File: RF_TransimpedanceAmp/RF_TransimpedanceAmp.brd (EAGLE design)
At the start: 22.9 x 22.9 mm, 11 parts, among them IC1 OPA847, IC3 PMA-5452, X1 UMC

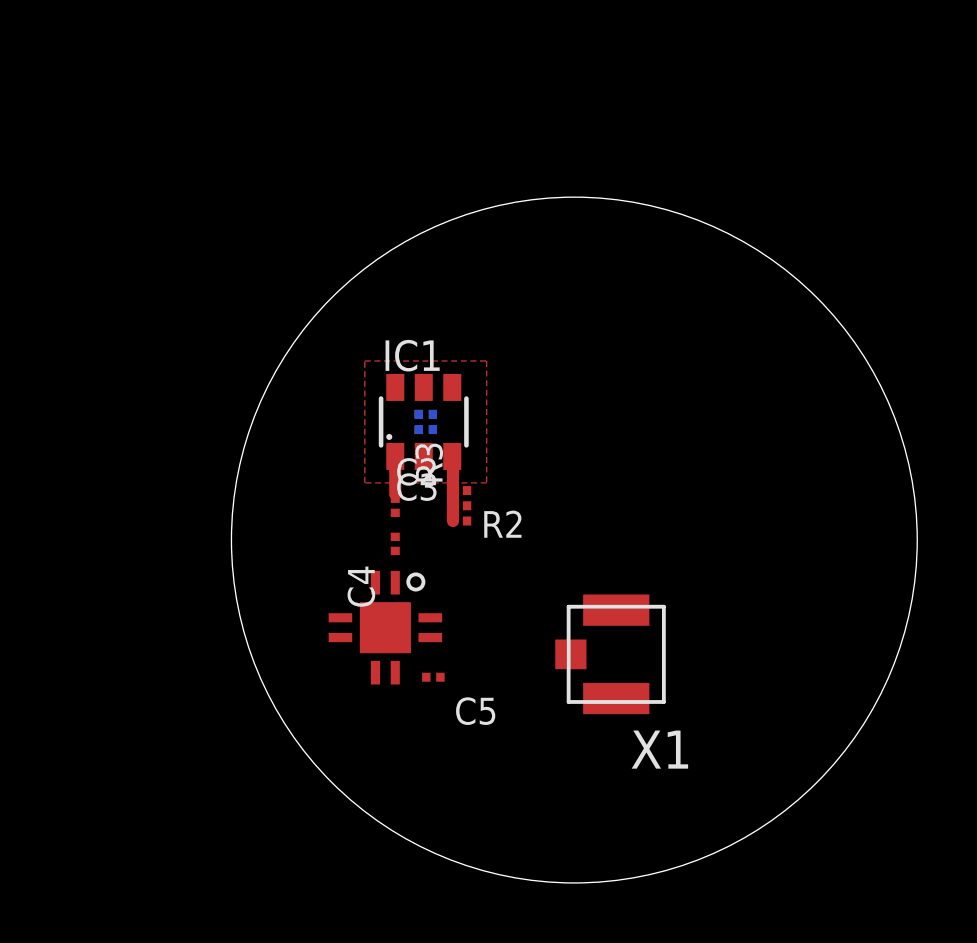
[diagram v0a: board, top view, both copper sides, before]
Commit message: Schematic done; routing in progress. Want to check with alessandro.
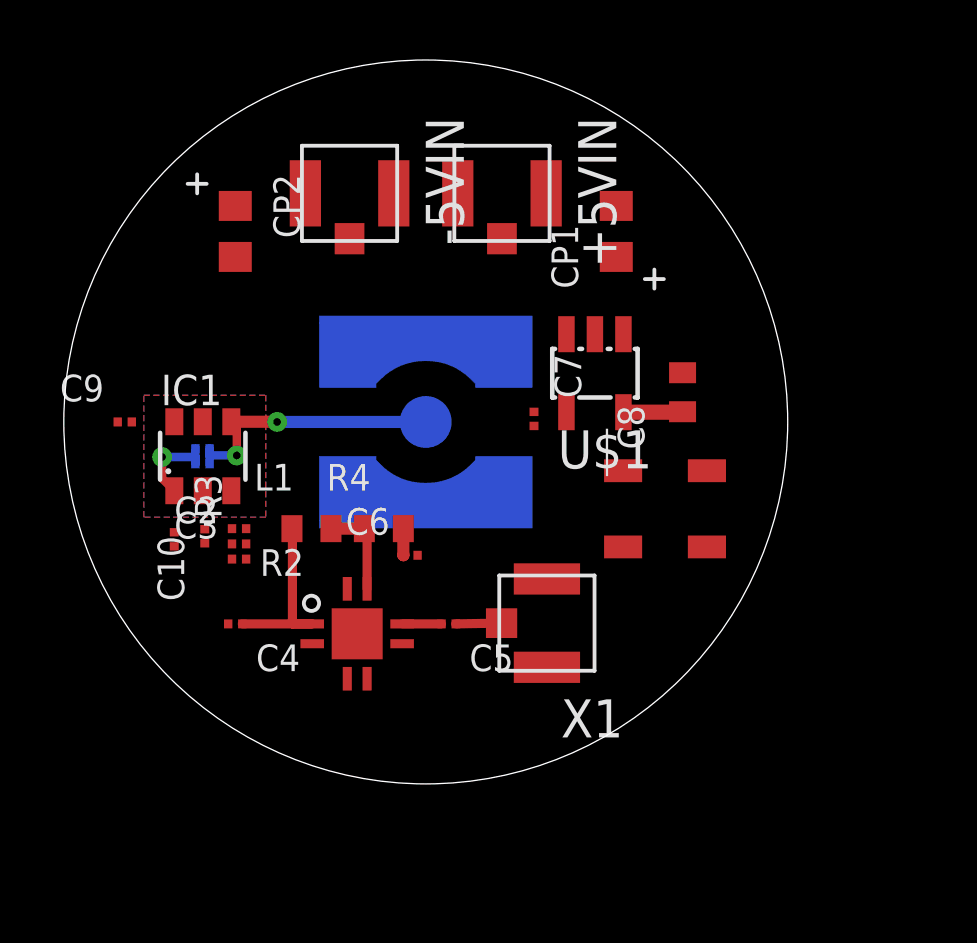
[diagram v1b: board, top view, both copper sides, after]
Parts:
- added +5VIN, -5VIN: UMC, connector-jqi:UMC
- added C10, C6, C9: 100nF, rlc-jqi:0201
- added C7: 470pF, rlc-jqi:0201
- added C8: 2.2uF, rlc-jqi:0402
- added CH1: TCCH-80, rf-jqi:GU1604
- added CP1, CP2: (no value), rlc-jqi:0603P
- added L1: 390nH, rlc-jqi:0402
- added PD: SMA, connector-jqi:SMA-SMT
- added R4: 1k, rlc-jqi:0402
- added U$1: MIC5205, regulator-jqi:SOT23-5L
- C4, C5: value (none) -> 100nF
- moved C1 7.53 mm to (-7.44, -1.40)
- moved R1 7.53 mm to (-7.44, -0.89)
- moved C2 7.47 mm to (-6.22, -4.06)
- moved C3 7.47 mm to (-6.22, -4.57)
- moved R2 7.47 mm to (-6.22, -3.56)
- moved IC1 7.45 mm to (-8.38, -1.14)
- moved R3 7.45 mm to (-8.38, -3.91)
- moved C4 5.96 mm to (-6.35, -6.73), turned to 180 degrees
- moved X1 2.54 mm to (4.04, -6.71)
- moved C5 1.85 mm to (0.76, -6.73)
- moved IC3 1.28 mm to (-2.29, -6.73), turned to 0 degrees
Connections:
- removed net BIAS: IC3.P$7
- new net +3V: C6.P$1, C8.1, CH1.P$3, R4.2, U$1.5
- new net N$10: C7.P$1, U$1.4
- new net N$9: IC3.P$7, L1.2, R4.1
- net +5V: now also +5VIN.P$1, C9.P$2, CP1.1, U$1.1, U$1.3
- net -5V: now also -5VIN.P$1, C10.P$2, CP2.2
- net GND: now also C10.P$1, C6.P$2, C7.P$2, C8.2, C9.P$1, CP1.2, CP2.1, U$1.2
- net N$2: now also PD.P$1
- net N$5: now also L1.1
- net N$6: now also CH1.P$1
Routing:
- net N$2: track 0.00 -> 9.37 mm, vias 0 -> 2
- net N$5: track 0.00 -> 6.17 mm
- net N$9: track 0.00 -> 3.21 mm
- net +3V: track 0.00 -> 2.87 mm
- net N$1: track 2.18 -> 0.00 mm
- net N$3: track 1.41 -> 3.14 mm, vias 0 -> 1
- net N$7: track 0.00 -> 1.53 mm
- net N$6: track 0.00 -> 1.31 mm
- added copper zone on layer 16, net N$8
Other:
- board size 22.9 x 22.9 mm -> 24.1 x 24.1 mm
